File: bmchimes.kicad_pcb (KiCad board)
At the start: 2 copper layers, 63.5 x 50.8 mm, 28 parts, among them P1 CONN_01X10, P10 CONN_01X01, P11 CONN_01X01, P2 CONN_01X05, P3 CONN_02X03, P4 CONN_01X02, P5 CONN_01X06, P6 CONN_01X06, P7 CONN_01X02, P8 CONN_01X01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

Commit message: Zero unconnected nets, calling it done
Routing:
- net RESET: track 0.00 -> 102.2 mm, vias 0 -> 1
- net GPIO13: track 0.00 -> 68.3 mm
- net ADC: track 0.00 -> 48.1 mm, vias 0 -> 2
- net GPIO2_OUT: track 0.00 -> 47.2 mm, vias 0 -> 1
- net GPIO2: track 0.00 -> 41.9 mm
- net BATT: track 0.00 -> 36.0 mm
- net GPIO2_IN_ST: track 0.00 -> 35.5 mm, vias 0 -> 1
- net GPIO5: track 0.00 -> 35.1 mm, vias 0 -> 1
- net GPIO4: track 0.00 -> 33.9 mm, vias 0 -> 1
- net GPIO14_IN: track 0.00 -> 30.9 mm
- net TXD: track 0.00 -> 30.7 mm, vias 0 -> 1
- net RESET_SER: track 0.00 -> 28.8 mm
- net RXD: track 0.00 -> 26.6 mm, vias 0 -> 1
- net GPIO14: track 0.00 -> 26.2 mm, vias 0 -> 2
- net GPIO12: track 0.00 -> 24.4 mm, vias 0 -> 2
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
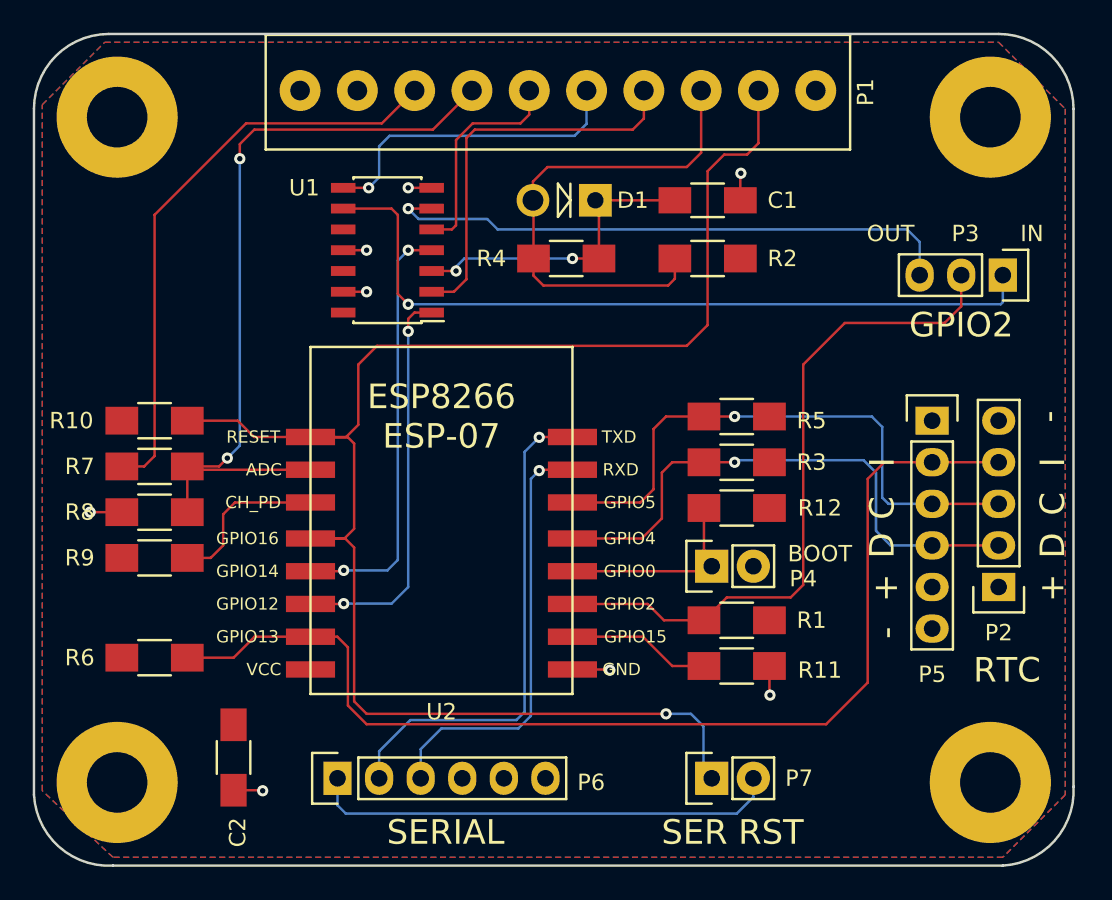
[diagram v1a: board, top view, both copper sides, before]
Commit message: Silkscreen changes, sent board to OSH Park
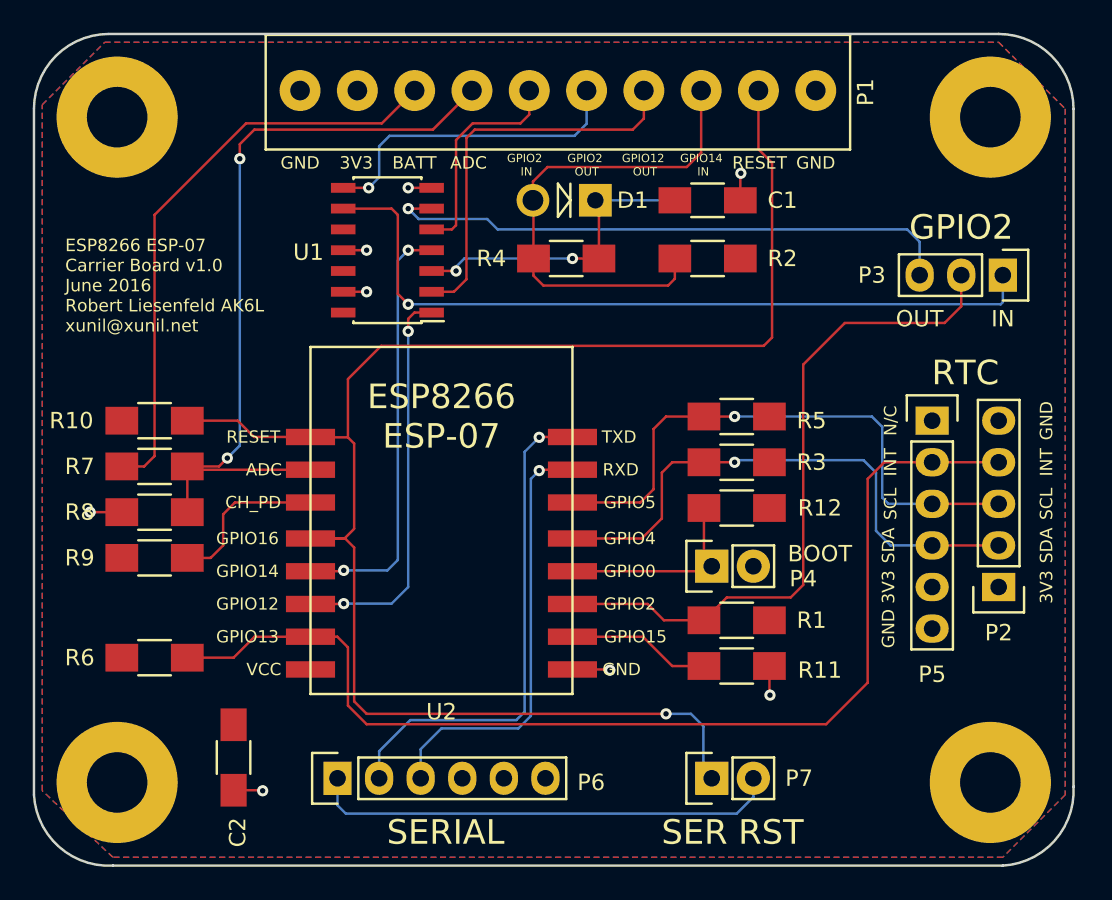
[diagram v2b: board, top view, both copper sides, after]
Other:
- board text added: "3V3"
- board text added: "ADC"
- board text added: "BATT"
- board text added: "ESP8266 ESP-07 Carrier Board v1.0 June 2016 Robert Liesenfeld AK6L xunil@xunil.net"
- board text added: "GND"
- board text added: "GPIO12 OUT"
- board text added: "GPIO14 IN"
- board text added: "GPIO2 IN"
- board text added: "GPIO2 OUT"
- board text added: "INT"
- board text added: "N/C"
- board text added: "RESET"
- board text added: "SCL"
- board text added: "SDA"
- board text removed: "+"
- board text removed: "-"
- board text removed: "C"
- board text removed: "D"
- board text removed: "I"
